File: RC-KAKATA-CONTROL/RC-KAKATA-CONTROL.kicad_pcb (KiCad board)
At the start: 4 copper layers, 160 x 160 mm, 166 parts, among them J1 Conn_02x20_Socket_DG250T-5.0-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, J10 DB125-2.54-4P-GN, J11 Screw_Terminal_01x02, J12 Conn_01x07, J13 Screw_Terminal_01x02, J17 Screw_Terminal_01x02, J19 Screw_Terminal_01x02, J2 Screw_Terminal_01x02, J21 Screw_Terminal_01x02, J23 Screw_Terminal_01x02, J25 Conn_02x20_Socket_DG250T-5.0-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, J3 Screw_Terminal_01x02, J4 Screw_Terminal_01x02, J5 Screw_Terminal_01x02, J6 Raspberry_Pi_2x20_PTH, J7 Screw_Terminal_01x02, J8 DB125-2.54-4P-GN, J9 Screw_Terminal_01x02, SW1 TS-1088-AR02016, SW2 TS-1088-AR02016, SW3 TS-1088-AR02016, SW4 TS-1088-AR02016, SW6 TS-1088-AR02016, U1 PS-TO220, U13 ICM-20689, U2 PS-TO220, U3 STM32H743IIT6, U4 YK16S-L7.2-B10KA(32-8)-G-A29, U8 W25Q128JVSIQTR, X1 SMD3225-4, X2 Q13MC3061000300

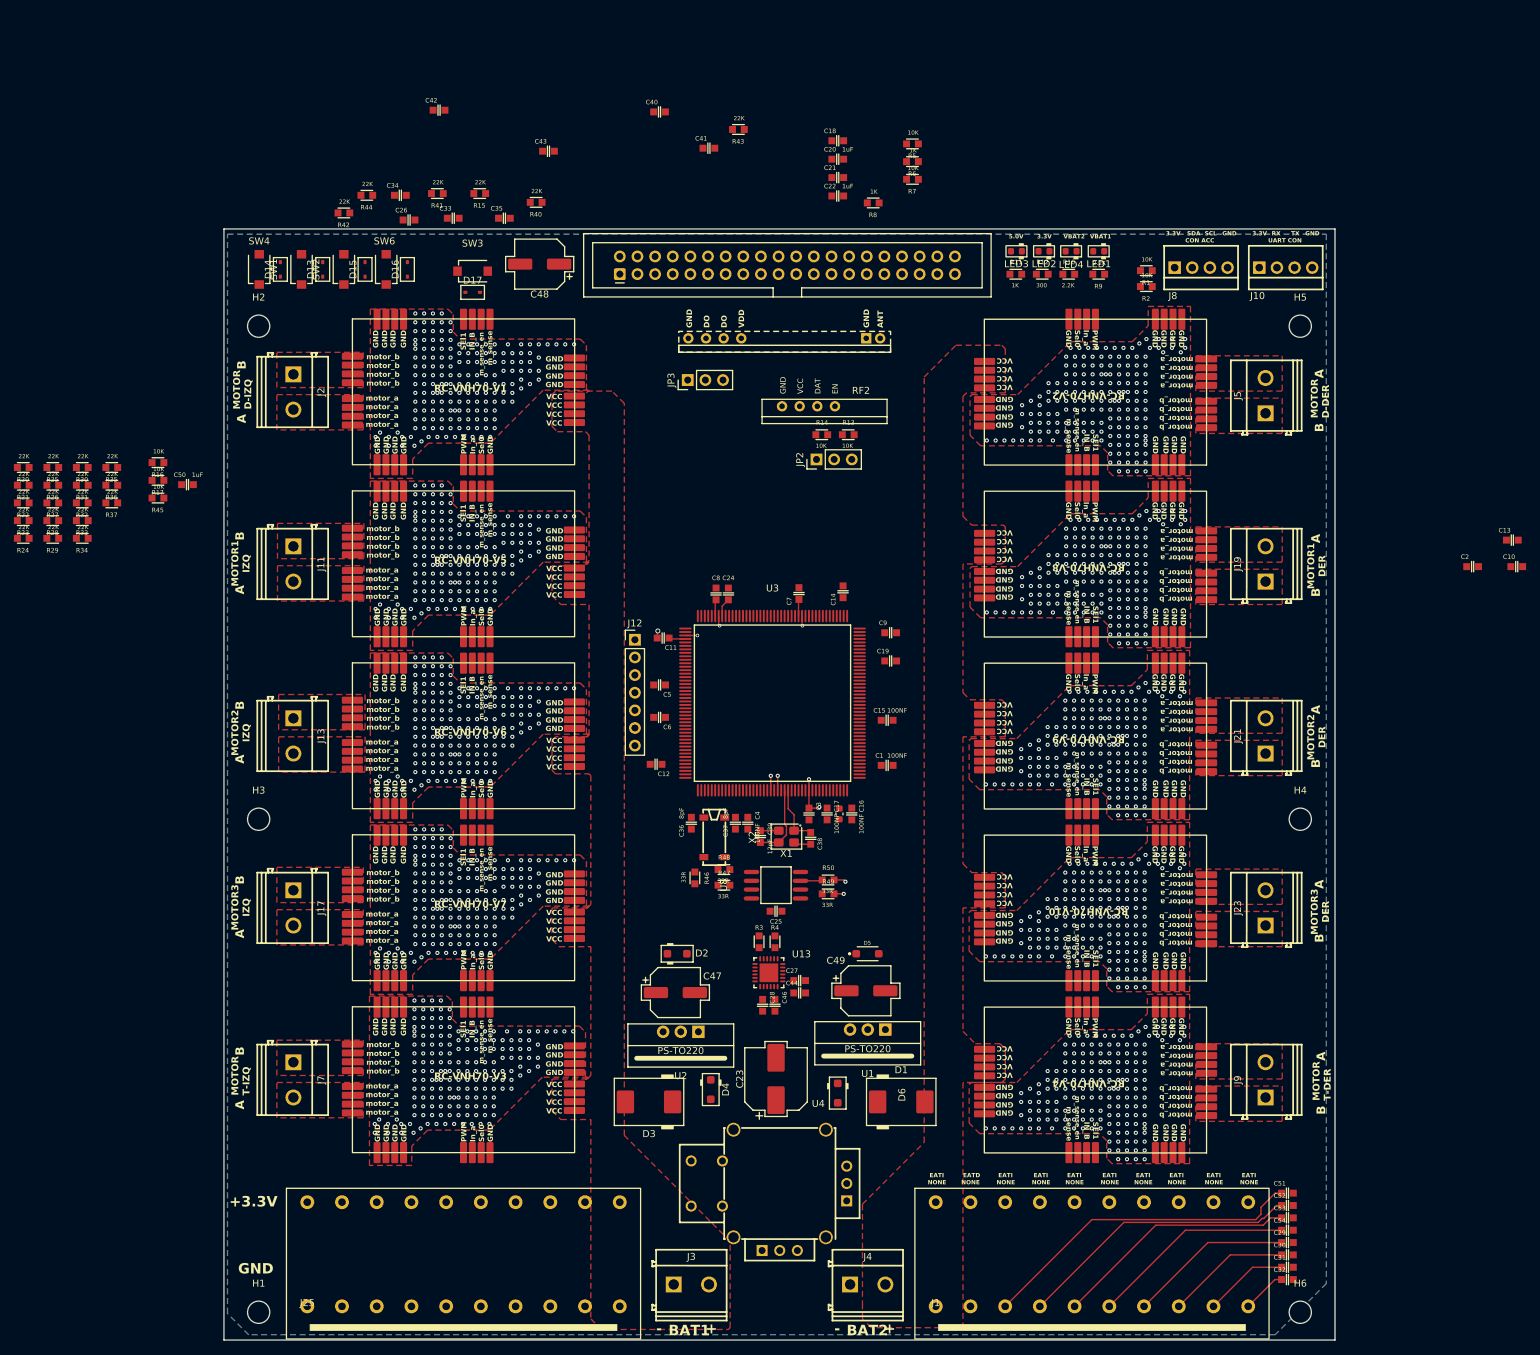
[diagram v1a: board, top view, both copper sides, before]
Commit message: Colocadas todas las piezas Verificacion de conexiones de los puertos UART - I2C - SPI Realizadas todas las conexiones Verificados los errores
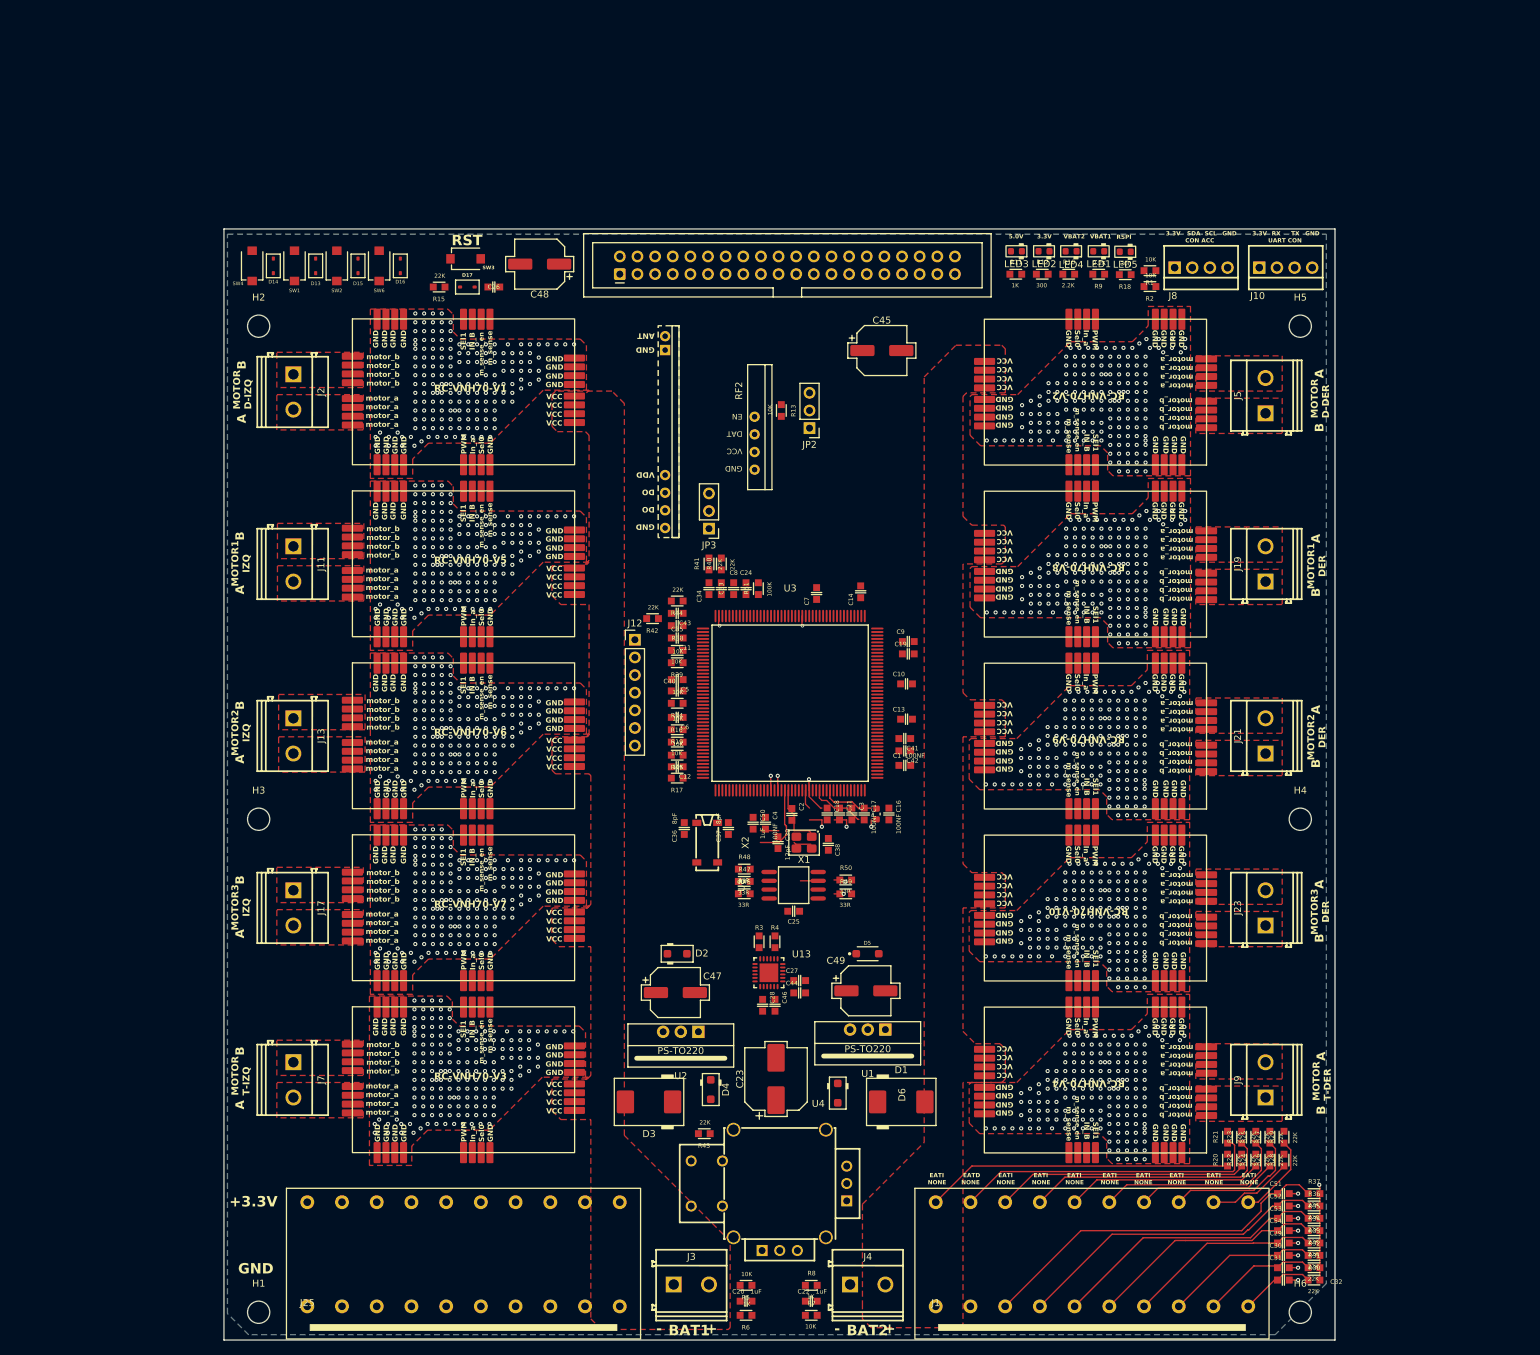
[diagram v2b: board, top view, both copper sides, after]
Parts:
- removed C15: 100NF, 4ms_Capacitor:C_0603
- added C45: 100uF, Capacitor_SMD_AKL:CP_Elec_6.3x5.9, F.Cu at (189.2, 75.5)
- added LED5: LED_0603_Red, LED_SMD_AKL:LED_0603_1608Metric, F.Cu at (224.3, 61.3)
- added R18: 300, 4ms_Resistor:R_0603, F.Cu at (224.3, 64.6)
- added R19: 10K, 4ms_Resistor:R_0603, F.Cu at (159.8, 130.1)
- added R38: 10K, 4ms_Resistor:R_0603, F.Cu at (159.8, 118.7)
- added R39: 10K, 4ms_Resistor:R_0603, F.Cu at (159.8, 120.5)
- added R51: 100K, 4ms_Resistor:R_0603, F.Cu at (171.5, 109.8)
- moved R30 212.5 mm to (251.5, 209.4), turned to 180 degrees
- moved R31 210.1 mm to (251.5, 207.6), turned to 180 degrees
- moved R32 207.9 mm to (251.5, 205.8), turned to 180 degrees
- moved R33 205.6 mm to (251.5, 204.0), turned to 180 degrees
- moved R35 204.1 mm to (251.5, 200.5), turned to 180 degrees
- moved R34 203.5 mm to (251.5, 202.3), turned to 180 degrees
- moved R36 201.9 mm to (251.5, 198.7), turned to 180 degrees
- moved R26 200.4 mm to (245.1, 192.1), turned to -90 degrees
- moved R20 200.1 mm to (239.0, 192.1), turned to -90 degrees
- moved R28 199.8 mm to (247.2, 192.1), turned to -90 degrees
- moved R37 199.7 mm to (251.5, 196.9), turned to 180 degrees
- moved R22 199.4 mm to (241.1, 192.1), turned to -90 degrees
- moved R24 198.8 mm to (243.1, 192.1), turned to -90 degrees
- moved R25 198.3 mm to (243.1, 188.8), turned to -90 degrees
- moved R27 197.6 mm to (245.1, 188.8), turned to -90 degrees
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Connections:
- C26 pad 1: /NJTRST -> /nrst
- D17 pad 2: /NJTRST -> /nrst
- J12 pad 4: /NJTRST -> /JTDI
- J12 pad 5: /JTDI -> /NJTRST
- J6 pad 11: unconnected-(J6-GPIO17-Pad11) -> /RPI_GPIO_17
- J6 pad 12: unconnected-(J6-GPIO18/PWM0-Pad12) -> /RPI_GPIO_18
- J6 pad 3: unconnected-(J6-SDA/GPIO2-Pad3) -> /RPI_GPIO_SDA
- J6 pad 36: unconnected-(J6-GPIO16-Pad36) -> /RPI_GPIO_16
- J6 pad 5: unconnected-(J6-SCL/GPIO3-Pad5) -> /RPI_GPIO_SCL
- R14 pad 2: /RF_TRANSMITTER/RF_TRANSMITER_EN -> /RF_DATA_EN
- R15 pad 2: /NJTRST -> /nrst
- RF2 pad 2: /RF_TRANSMITTER/RF_TRANSMITER_EN -> /RF_DATA_EN
- SW3 pad 2: /NJTRST -> /nrst
- U3 pad 1: unconnected-(U3-PE2-Pad1) -> /RF_DATA_IN_TIM
- U3 pad 119: unconnected-(U3-PA8-Pad119) -> /RPI_GPIO_16
- U3 pad 120: unconnected-(U3-PA9-Pad120) -> /RPI_GPIO_17
- U3 pad 121: unconnected-(U3-PA10-Pad121) -> /RPI_GPIO_18
- U3 pad 128: unconnected-(U3-PH13-Pad128) -> /RF_DATA_UART_TX
- U3 pad 129: unconnected-(U3-PH14-Pad129) -> /RF_DATA_IN_UART
- U3 pad 157: unconnected-(U3-PG14-Pad157) -> /RF_DATA_EN
- U3 pad 2: unconnected-(U3-PE3-Pad2) -> /RF_DATA_TIMER
- U3 pad 32: unconnected-(U3-PC0-Pad32) -> /ADC_VBAT1
- U3 pad 33: unconnected-(U3-PC1-Pad33) -> /ADC_VBAT2
- U3 pad 38: unconnected-(U3-VREF+-Pad38) -> VDDA
- U3 pad 50: unconnected-(U3-PA4-Pad50) -> /RPI_SPI_CS
- U3 pad 51: unconnected-(U3-PA5-Pad51) -> /RPI_SPI_CLK
- U3 pad 52: unconnected-(U3-PA6-Pad52) -> /RPI_SPI_MOSI
- U3 pad 53: unconnected-(U3-PA7-Pad53) -> /RPI_SPI_MISO
- U3 pad 84: unconnected-(U3-PH7-Pad84) -> /RPI_GPIO_SCL
- U3 pad 85: unconnected-(U3-PH8-Pad85) -> /RPI_GPIO_SDA
- U3 pad 96: unconnected-(U3-PD8-Pad96) -> /RPI_UART2_RX
- U3 pad 97: unconnected-(U3-PD9-Pad97) -> /RPI_UART2_TX
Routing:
- net /ENC_A_TRASERO_DER: track 0.00 -> 44.7 mm
- net /ENC_A_TRASERO_IZQ: track 0.00 -> 44.2 mm
- net /ENC_A_DELANTERO_IZQ: track 0.00 -> 36.3 mm
- net /ENC_A_DELANTERO_DER: track 0.00 -> 36.0 mm
- net /ENC_A_MOTOR_1_IZQ: track 0.00 -> 28.2 mm
- net /ENC_A_MOTOR_2_IZQ: track 0.00 -> 28.1 mm
- net /ENC_A_MOTOR_3_IZQ: track 0.00 -> 20.3 mm
- net /ENC_A_MOTOR_1_DER: track 0.00 -> 20.1 mm
- net /ENC_A_MOTOR_2_DER: track 0.00 -> 12.3 mm
- net /ENC_A_MOTOR_3_DER: track 0.00 -> 12.3 mm
- net /FLASH_IO_1: track 31.1 -> 42.6 mm
- net GND: track 11.0 -> 21.8 mm, vias 1744 -> 1751
- net +3.3V: track 12.9 -> 21.8 mm, vias 2 -> 1
- net /XTAL_25M_OUT: track 8.67 -> 0.00 mm
- net VDDA: track 0.00 -> 7.74 mm
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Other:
- board text added: "RSPI"
- board text added: "RST"
